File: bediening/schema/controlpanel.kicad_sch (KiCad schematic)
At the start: 19 parts, among them J1 SW1, J2 SW2, J3 SW3, J4 SPI Display, J5 SW4, J6 SW35

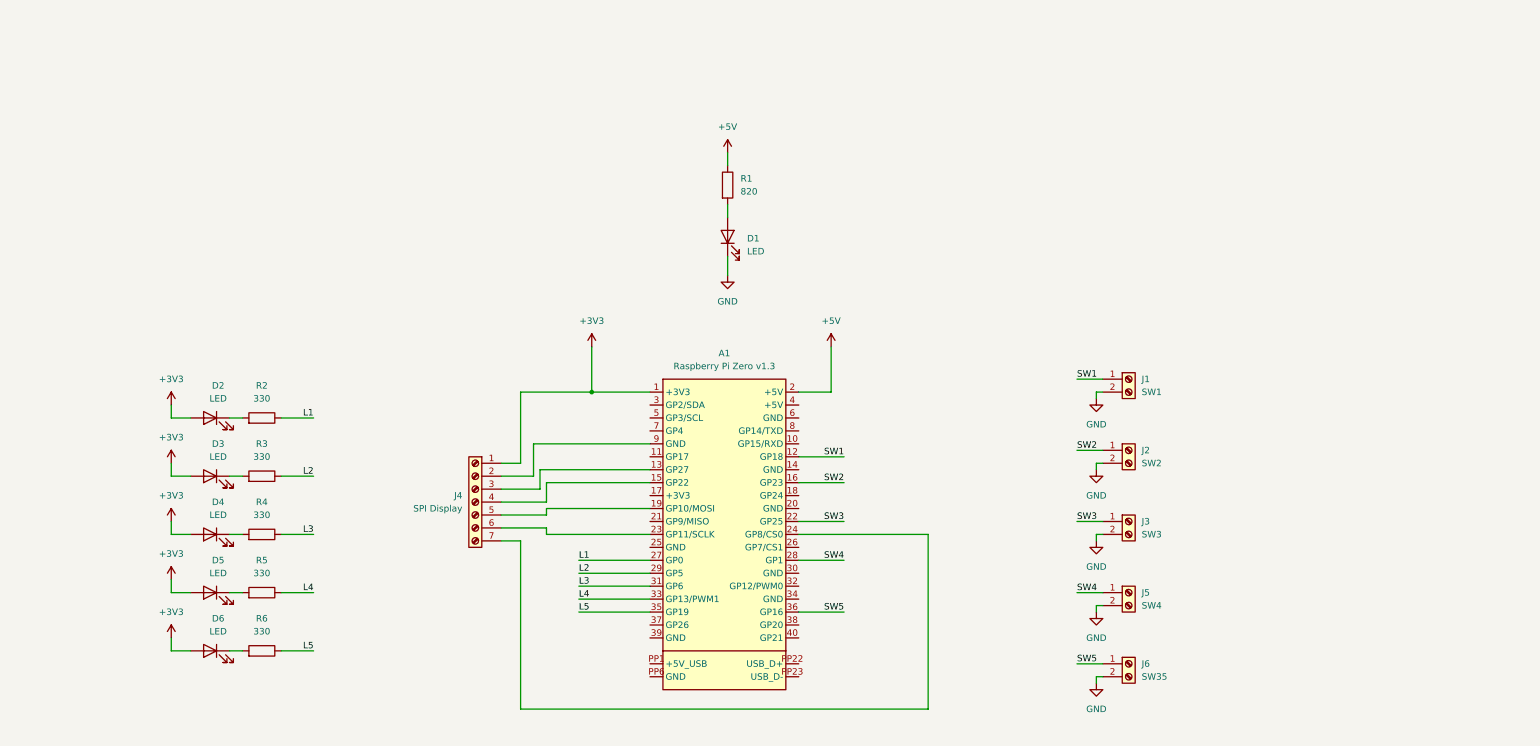
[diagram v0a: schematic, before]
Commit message: Add rotary knob
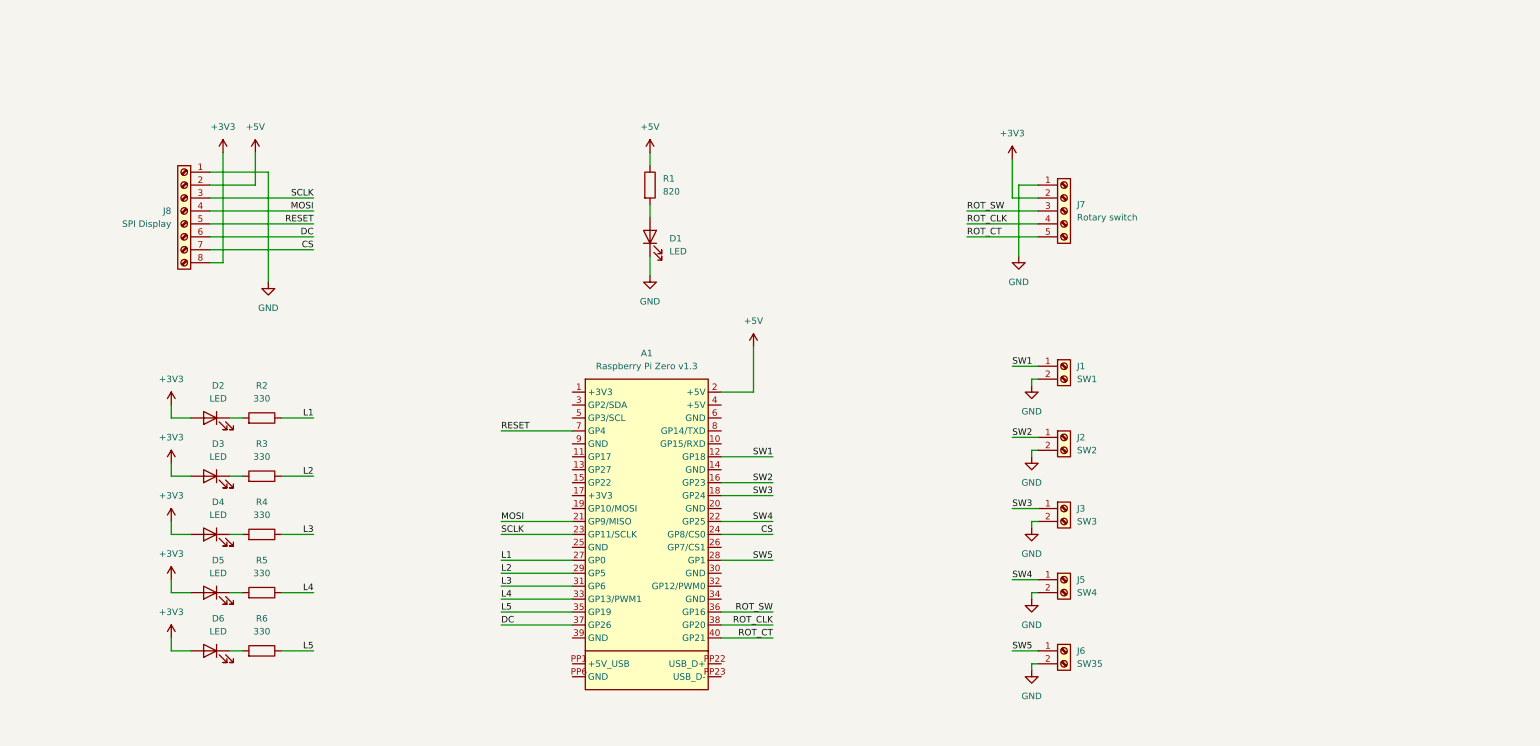
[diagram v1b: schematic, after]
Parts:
- removed J4: SPI Display, symbol Connector:Screw_Terminal_01x07
- added J7: Rotary switch, symbol Connector:Screw_Terminal_01x05
- added J8: SPI Display, symbol Connector:Screw_Terminal_01x08
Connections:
- net +3V3: now also J7.2 (Pin_2), J8.8 (Pin_8); no longer A1.1 (+3V3)
- net +5V: now also J8.2 (Pin_2)
- net GND: now also J7.1 (Pin_1), J8.1 (Pin_1)
- net SW3: now also A1.18 (GP24); no longer A1.22 (GP25)
- net SW4: now also A1.22 (GP25); no longer A1.28 (GP1)
- net SW5: now also A1.28 (GP1); no longer A1.36 (GP16)
- net MOSI: now reaches A1.21 (GP9/MISO)
- net MOSI: now also J8.4 (Pin_4)
- net SCLK: now reaches A1.23 (GP11/SCLK)
- net SCLK: now also J8.3 (Pin_3)
- net CS: now reaches A1.24 (GP8/CS0)
- net CS: now also J8.7 (Pin_7)
- net DC: now reaches A1.37 (GP26)
- net DC: now also J8.6 (Pin_6)
- net ROT_CLK: now reaches A1.38 (GP20)
- net ROT_CLK: now also J7.4 (Pin_4)
- net ROT_CT: now reaches A1.40 (GP21)
- net ROT_CT: now also J7.5 (Pin_5)
- net RESET: now reaches A1.7 (GP4)
- net RESET: now also J8.5 (Pin_5)
- new net ROT_SW: A1.36 (GP16), J7.3 (Pin_3)
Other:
- moved on the sheet: A1, D1, J1, J2, J3, J5, J6, R1

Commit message: pcb update
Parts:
- removed A1: Raspberry Pi Zero v1.3, Raspberry_Pi_Zero_v.1.3_Hat:RASPI_ZERO_FULL, symbol Pi:Raspberry_Pi_Zero_v.1.3_Hat
- added A2: Arduino_Nano_ESP32, Module:Arduino_Nano, symbol MCU_Module:Arduino_Nano_ESP32
- R1, R2, R3, R4, R5, R6: footprint (none) -> Resistor_THT:R_Axial_DIN0204_L3.6mm_D1.6mm_P7.62mm_Horizontal
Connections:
- net +5V: now also A2.30 (VIN)
- net CS: now also A2.13 (D10/CS)
- net DC: now also A2.12 (D9)
- net L1: now also A2.21 (A2)
- net L2: now also A2.22 (A3)
- net L3: now also A2.23 (SDA/A4)
- net L4: now also A2.24 (SCL/A5)
- net L5: now also A2.25 (A6)
- net MOSI: now also A2.14 (D11/COPI)
- net ROT_CLK: now also A2.19 (A0)
- net ROT_CT: now also A2.20 (A1)
- net ROT_SW: now also A2.10 (D7)
- net SCLK: now also A2.16 (D13/SCK)
- net SW1: now also A2.5 (D2)
- net SW2: now also A2.6 (D3)
- net SW3: now also A2.7 (D4)
- net SW4: now also A2.8 (D5)
- net SW5: now also A2.9 (D6)
- net RESET renamed DISPLAY_RESET
- net DISPLAY_RESET: now also A2.11 (D8)
- new net: A2.29 (GND), A2.4 (GND)
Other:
- moved on the sheet: D1, R1

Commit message: Fix up
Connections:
- net +3V3: now also A2.17 (3V3)
- net GND: now also A2.29 (GND), A2.4 (GND)
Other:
- moved on the sheet: D1, R1

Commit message: pcb update
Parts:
- removed A2: Arduino_Nano_ESP32, Module:Arduino_Nano, symbol MCU_Module:Arduino_Nano_ESP32
- removed D1, D2, D3, D4, D5, D6: LED, symbol Device:LED
- removed J1: SW1, symbol Connector:Screw_Terminal_01x02
- removed J2: SW2, symbol Connector:Screw_Terminal_01x02
- removed J3: SW3, symbol Connector:Screw_Terminal_01x02
- removed J5: SW4, symbol Connector:Screw_Terminal_01x02
- removed J6: SW35, symbol Connector:Screw_Terminal_01x02
- removed R1: 820, Resistor_THT:R_Axial_DIN0204_L3.6mm_D1.6mm_P7.62mm_Horizontal, symbol Device:R
- removed R2, R3, R4, R5, R6: 330, Resistor_THT:R_Axial_DIN0204_L3.6mm_D1.6mm_P7.62mm_Horizontal, symbol Device:R
- added A1: Arduino_Nano_ESP32, Module:Arduino_Nano, symbol MCU_Module:Arduino_Nano_ESP32
- added C1: 0.1uF, Capacitor_THT:C_Disc_D5.0mm_W2.5mm_P5.00mm, symbol PCM_SparkFun-Capacitor:0.1uF_0402_16V_10%
- added C3: 470uF, Capacitor_THT:CP_Radial_D8.0mm_P3.50mm, symbol PCM_SparkFun-Capacitor:470uF_10x10_25V_20%
- added J1: Leds, Connector_PinHeader_2.54mm:PinHeader_1x14_P2.54mm_Vertical, symbol Connector:Conn_01x14_Pin
- added J2: Schakelaars, Connector_PinHeader_2.54mm:PinHeader_1x14_P2.54mm_Vertical, symbol Connector:Conn_01x14_Pin
- added J4: Power, TerminalBlock_Phoenix:TerminalBlock_Phoenix_MKDS-1,5-2-5.08_1x02_P5.08mm_Horizontal, symbol Connector:Screw_Terminal_01x02
- added R10, R12, R13, R14, R15, R16, R17, R18, R19, R20, R7, R8, R9: 330, Resistor_THT:R_Axial_DIN0204_L3.6mm_D1.6mm_P7.62mm_Horizontal, symbol Device:R
- added R11: 10k, Resistor_THT:R_Axial_DIN0204_L3.6mm_D1.6mm_P7.62mm_Horizontal, symbol Device:R
- added R61, R62: 4k7, Resistor_THT:R_Axial_DIN0204_L3.6mm_D1.6mm_P7.62mm_Horizontal, symbol Device:R
- added U1: MCP23017x-x-SP, Package_DIP:DIP-28_W7.62mm, symbol Interface_Expansion:MCP23017x-x-SP
- J7: footprint (none) -> Connector_PinHeader_2.54mm:PinHeader_1x05_P2.54mm_Vertical
- J8: footprint (none) -> Connector_PinHeader_2.54mm:PinHeader_1x08_P2.54mm_Vertical
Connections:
- net +3V3: now also J1.13 (Pin_13), J2.13 (Pin_13)
- net +5V: now also A1.30 (VIN), C3.1, J4.2 (Pin_2)
- net CS: now also A1.13 (D10/CS)
- net DC: now also A1.12 (D9)
- net DISPLAY_RESET: now also A1.11 (D8)
- net GND: now also A1.29 (GND), A1.4 (GND), C1.1, C3.2, J2.14 (Pin_14), J4.1 (Pin_1), R20.1, U1.10 (V_{SS}), U1.15 (A0), U1.16 (A1), U1.17 (A2)
- net L1: now also R7.1, U1.21 (GPA0)
- net L2: now also R8.1, U1.22 (GPA1)
- net L3: now also R9.1, U1.23 (GPA2)
- net L4: now also R10.1, U1.24 (GPA3)
- net L5: now also R12.1, U1.25 (GPA4)
- net MOSI: now also A1.14 (D11/COPI)
- net ROT_CLK: now also A1.19 (A0)
- net ROT_CT: now also A1.20 (A1)
- net ROT_SW: now also A1.10 (D7)
- net SCLK: now also A1.16 (D13/SCK)
- net SW1: now also J2.1 (Pin_1), U1.1 (GPB0)
- net SW2: now also J2.2 (Pin_2), U1.2 (GPB1)
- net SW3: now also J2.3 (Pin_3), U1.3 (GPB2)
- net SW4: now also J2.4 (Pin_4), U1.4 (GPB3)
- net SW5: now also J2.5 (Pin_5), U1.5 (GPB4)
- new net: J1.7 (Pin_7), R14.2
- new net: J1.4 (Pin_4), R10.2
- new net: J1.2 (Pin_2), R8.2
- new net: R11.2, U1.18 (~{RESET})
- new net: J1.11 (Pin_11), R18.2
- new net: J1.8 (Pin_8), R15.2
- new net: J1.1 (Pin_1), R7.2
- new net: J1.6 (Pin_6), R13.2
- new net: J1.3 (Pin_3), R9.2
- new net: J1.10 (Pin_10), R17.2
- new net: J1.12 (Pin_12), R19.2
- new net: J1.14 (Pin_14), R20.2
- new net: J1.5 (Pin_5), R12.2
- new net: J1.9 (Pin_9), R16.2
- new net +3.3V: A1.17 (3V3), C1.2, R11.1, R61.1, R62.1, U1.9 (V_{DD})
- new net L10: A1.6 (D3), R17.1
- new net L11: A1.7 (D4), R18.1
- new net L12: A1.8 (D5), R19.1
- new net L6: R13.1, U1.26 (GPA5)
- new net L7: R14.1, U1.27 (GPA6)
- new net L8: R15.1, U1.28 (GPA7)
- new net L9: A1.5 (D2), R16.1
- new net SCL: A1.24 (SCL/A5), R61.2, U1.12 (SCK)
- new net SDA: A1.23 (SDA/A4), R62.2, U1.13 (SDA)
- new net SW10: A1.22 (A3), J2.10 (Pin_10)
- new net SW11: A1.25 (A6), J2.11 (Pin_11)
- new net SW12: A1.26 (A7), J2.12 (Pin_12)
- new net SW6: J2.6 (Pin_6), U1.6 (GPB5)
- new net SW7: J2.7 (Pin_7), U1.7 (GPB6)
- new net SW8: J2.8 (Pin_8), U1.8 (GPB7)
- new net SW9: A1.21 (A2), J2.9 (Pin_9)
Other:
- moved on the sheet: J7, J8
